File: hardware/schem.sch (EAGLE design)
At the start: 19 parts, among them IC1 7805L, IC2 L298, U2 TINY85-20-DIP

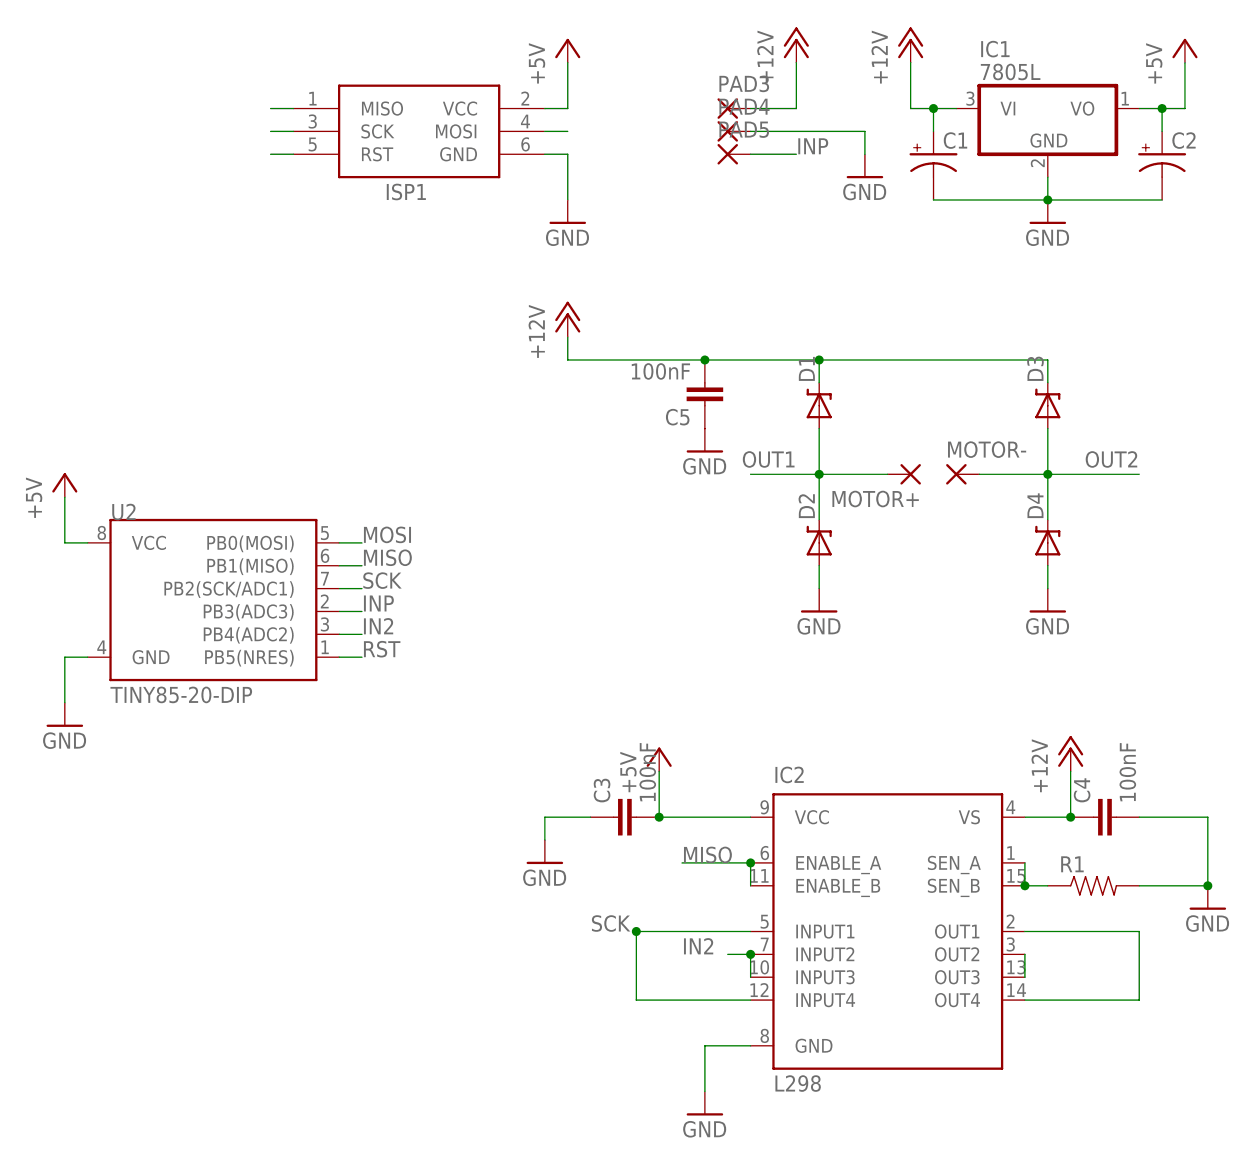
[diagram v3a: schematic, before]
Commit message: Routed board
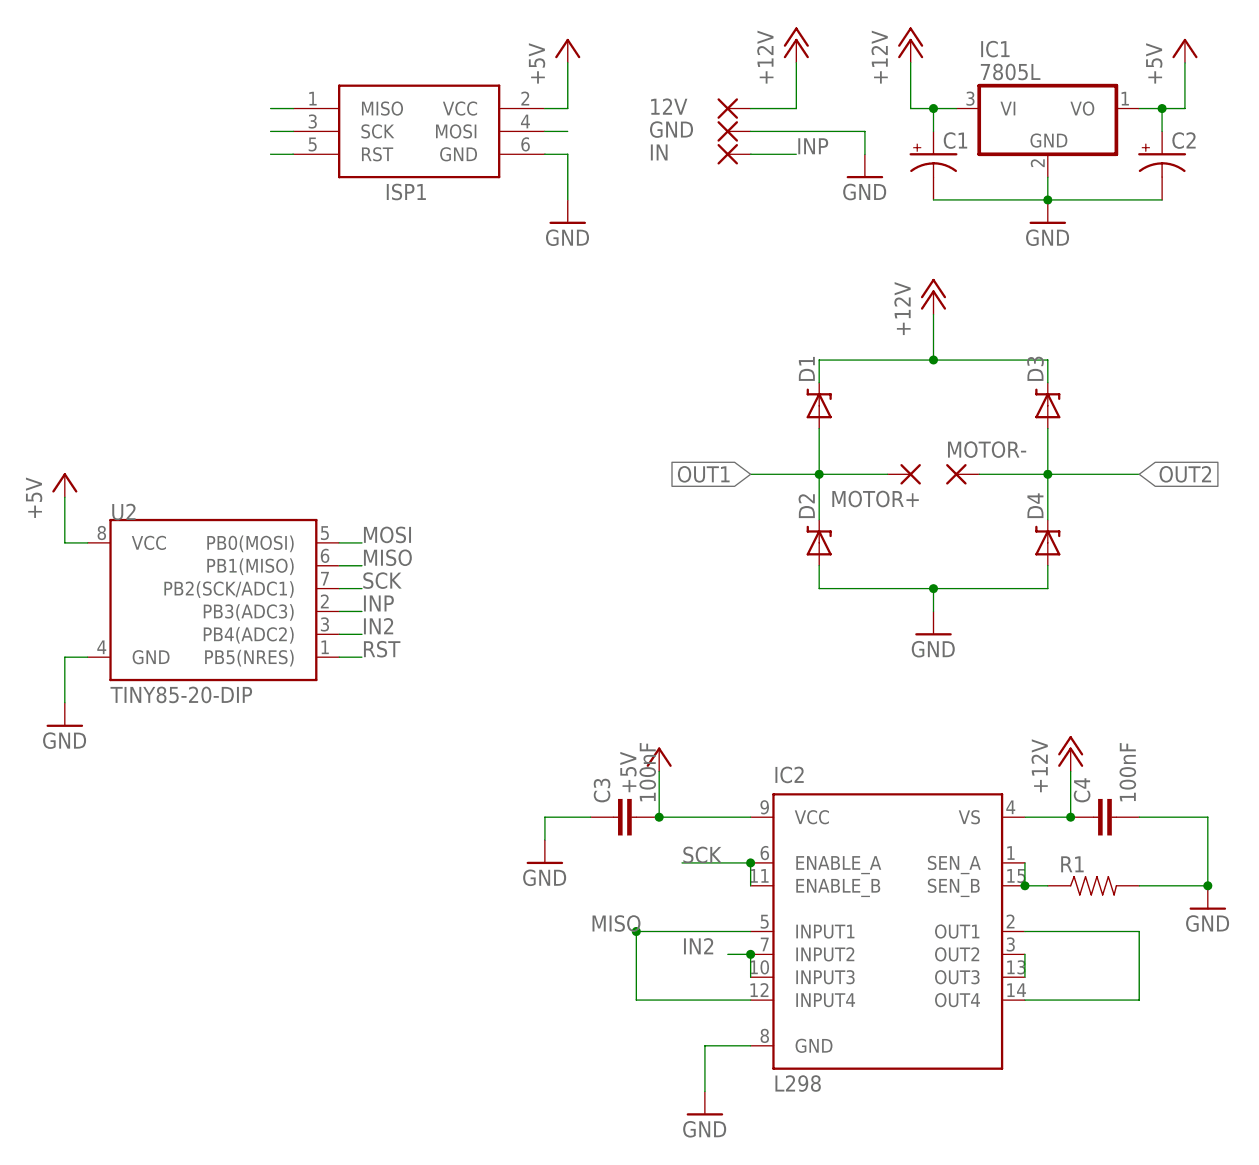
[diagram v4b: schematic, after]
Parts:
- removed C5: 100nF, SparkFun-Capacitors:CAPPTH2
- renumbered PAD3 to 12V, PAD4 to GND, PAD5 to IN
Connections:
- net +12V: no longer C5.2
- net GND: no longer C5.1
- net MISO: now also IC2.INPUT1, IC2.INPUT4; no longer IC2.ENABLE_A, IC2.ENABLE_B
- net SCK: now also IC2.ENABLE_A, IC2.ENABLE_B; no longer IC2.INPUT1, IC2.INPUT4
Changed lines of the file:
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@@
 <part name="MOTOR+" library="wirepad" deviceset="3,81/1,4" device=""/>
 <part name="MOTOR-" library="wirepad" deviceset="3,81/1,4" device=""/>
-<part name="PAD3" library="wirepad" deviceset="3,81/1,4" device=""/>
-<part name="PAD4" library="wirepad" deviceset="3,81/1,4" device=""/>
-<part name="PAD5" library="wirepad" deviceset="1,6/0,9" device=""/>
+<part name="12V" library="wirepad" deviceset="3,81/1,4" device=""/>
+<part name="GND" library="wirepad" deviceset="3,81/1,4" device=""/>
+<part name="IN" library="wirepad" deviceset="1,6/0,9" device=""/>
 <part name="C1" library="adafruit" deviceset="CPOL-US" device="E2.5-6"/>
 <part name="C2" library="adafruit" deviceset="CPOL-US" device="E2.5-6"/>
@@
 <part name="D3" library="SparkFun-DiscreteSemi" deviceset="DIODE-ZENER" device="PTH"/>
 <part name="D4" library="SparkFun-DiscreteSemi" deviceset="DIODE-ZENER" device="PTH"/>
+<part name="P+8" library="supply1" deviceset="+12V" device=""/>
 <part name="GND8" library="supply1" deviceset="GND" device=""/>
-<part name="GND9" library="supply1" deviceset="GND" device=""/>
-<part name="C5" library="SparkFun-Capacitors" deviceset="CAP" device="PTH2" value="100nF"/>
-<part name="GND10" library="supply1" deviceset="GND" device=""/>
-<part name="P+8" library="supply1" deviceset="+12V" device=""/>
 </parts>
 <sheets>
@@
 <instance part="MOTOR+" gate="1" x="149.86" y="58.42" rot="R180"/>
 <instance part="MOTOR-" gate="1" x="154.94" y="58.42"/>
-<instance part="PAD3" gate="1" x="129.54" y="99.06"/>
-<instance part="PAD4" gate="1" x="129.54" y="96.52"/>
-<instance part="PAD5" gate="1" x="129.54" y="93.98"/>
+<instance part="12V" gate="1" x="129.54" y="99.06" smashed="yes">
+<attribute name="NAME" x="120.777" y="98.3742" size="1.778" layer="95"/>
+<attribute name="VALUE" x="128.397" y="95.758" size="1.778" layer="96"/>
+</instance>
+<instance part="GND" gate="1" x="129.54" y="96.52" smashed="yes">
+<attribute name="NAME" x="120.777" y="95.8342" size="1.778" layer="95"/>
+<attribute name="VALUE" x="128.397" y="93.218" size="1.778" layer="96"/>
+</instance>
+<instance part="IN" gate="1" x="129.54" y="93.98" smashed="yes">
+<attribute name="NAME" x="120.777" y="93.2942" size="1.778" layer="95"/>
+<attribute name="VALUE" x="128.397" y="90.678" size="1.778" layer="96"/>
+</instance>
 <instance part="C1" gate="G$1" x="152.4" y="93.98"/>
 <instance part="C2" gate="G$1" x="177.8" y="93.98"/>
@@
 <attribute name="NAME" x="164.6174" y="53.34" size="1.778" layer="95" rot="R90"/>
 </instance>
-<instance part="GND8" gate="1" x="139.7" y="43.18"/>
-<instance part="GND9" gate="1" x="165.1" y="43.18"/>
-<instance part="C5" gate="G$1" x="127" y="68.58" rot="R180"/>
-<instance part="GND10" gate="1" x="127" y="60.96"/>
-<instance part="P+8" gate="1" x="111.76" y="76.2"/>
+<instance part="P+8" gate="1" x="152.4" y="78.74"/>
+<instance part="GND8" gate="1" x="152.4" y="40.64"/>
 </instances>
 <busses>
@@
 <wire x1="137.16" y1="104.14" x2="137.16" y2="99.06" width="0.1524" layer="91"/>
 <wire x1="137.16" y1="99.06" x2="132.08" y2="99.06" width="0.1524" layer="91"/>
-<pinref part="PAD3" gate="1" pin="P"/>
+<pinref part="12V" gate="1" pin="P"/>
 </segment>
 <segment>
@@
 <pinref part="D3" gate="G$1" pin="C"/>
 <wire x1="165.1" y1="68.58" x2="165.1" y2="71.12" width="0.1524" layer="91"/>
-<wire x1="165.1" y1="71.12" x2="139.7" y2="71.12" width="0.1524" layer="91"/>
-<wire x1="127" y1="71.12" x2="139.7" y2="71.12" width="0.1524" layer="91"/>
+<wire x1="165.1" y1="71.12" x2="152.4" y2="71.12" width="0.1524" layer="91"/>
+<wire x1="152.4" y1="71.12" x2="152.4" y2="76.2" width="0.1524" layer="91"/>
+<pinref part="P+8" gate="1" pin="+12V"/>
 <pinref part="D1" gate="G$1" pin="C"/>
 <wire x1="139.7" y1="68.58" x2="139.7" y2="71.12" width="0.1524" layer="91"/>
-<junction x="139.7" y="71.12"/>
-<pinref part="C5" gate="G$1" pin="2"/>
-<wire x1="127" y1="71.12" x2="111.76" y2="71.12" width="0.1524" layer="91"/>
-<junction x="127" y="71.12"/>
-<wire x1="111.76" y1="71.12" x2="111.76" y2="73.66" width="0.1524" layer="91"/>
-<pinref part="P+8" gate="1" pin="+12V"/>
+<wire x1="152.4" y1="71.12" x2="139.7" y2="71.12" width="0.1524" layer="91"/>
+<junction x="152.4" y="71.12"/>
 </segment>
 </net>
@@
 <pinref part="GND1" gate="1" pin="GND"/>
 <wire x1="144.78" y1="96.52" x2="144.78" y2="93.98" width="0.1524" layer="91"/>
-<pinref part="PAD4" gate="1" pin="P"/>
+<pinref part="GND" gate="1" pin="P"/>
 </segment>
 <segment>
@@
 </segment>
 <segment>
+<pinref part="D4" gate="G$1" pin="A"/>
+<wire x1="165.1" y1="48.26" x2="165.1" y2="45.72" width="0.1524" layer="91"/>
 <pinref part="D2" gate="G$1" pin="A"/>
 <wire x1="139.7" y1="48.26" x2="139.7" y2="45.72" width="0.1524" layer="91"/>
+<wire x1="165.1" y1="45.72" x2="152.4" y2="45.72" width="0.1524" layer="91"/>
 <pinref part="GND8" gate="1" pin="GND"/>
-</segment>
-<segment>
-<pinref part="D4" gate="G$1" pin="A"/>
-<wire x1="165.1" y1="48.26" x2="165.1" y2="45.72" width="0.1524" layer="91"/>
-<pinref part="GND9" gate="1" pin="GND"/>
-</segment>
-<segment>
-<pinref part="C5" gate="G$1" pin="1"/>
-<pinref part="GND10" gate="1" pin="GND"/>
+<wire x1="152.4" y1="45.72" x2="139.7" y2="45.72" width="0.1524" layer="91"/>
+<wire x1="152.4" y1="45.72" x2="152.4" y2="43.18" width="0.1524" layer="91"/>
+<junction x="152.4" y="45.72"/>
 </segment>
 </net>
@@
 <wire x1="132.08" y1="93.98" x2="137.16" y2="93.98" width="0.1524" layer="91"/>
 <label x="137.16" y="93.98" size="1.778" layer="95"/>
-<pinref part="PAD5" gate="1" pin="P"/>
+<pinref part="IN" gate="1" pin="P"/>
 </segment>
 </net>
@@
 <pinref part="ISP1" gate="G$1" pin="MISO"/>
 <wire x1="78.74" y1="99.06" x2="81.28" y2="99.06" width="0.1524" layer="91"/>
-</segment>
-<segment>
-<pinref part="IC2" gate="L298" pin="ENABLE_A"/>
-<pinref part="IC2" gate="L298" pin="ENABLE_B"/>
-<wire x1="132.08" y1="15.24" x2="132.08" y2="12.7" width="0.1524" layer="91"/>
-<wire x1="132.08" y1="15.24" x2="124.46" y2="15.24" width="0.1524" layer="91"/>
-<junction x="132.08" y="15.24"/>
-<label x="124.46" y="15.24" size="1.778" layer="95"/>
-</segment>
-</net>
-<net name="RST" class="0">
-<segment>
-<pinref part="U2" gate="G$1" pin="PB5(NRES)"/>
-<wire x1="86.36" y1="38.1" x2="88.9" y2="38.1" width="0.1524" layer="91"/>
-<label x="88.9" y="38.1" size="1.778" layer="95"/>
-</segment>
-<segment>
-<pinref part="ISP1" gate="G$1" pin="RST"/>
-<wire x1="81.28" y1="93.98" x2="78.74" y2="93.98" width="0.1524" layer="91"/>
-</segment>
-</net>
-<net name="SCK" class="0">
-<segment>
-<pinref part="ISP1" gate="G$1" pin="SCK"/>
-<wire x1="81.28" y1="96.52" x2="78.74" y2="96.52" width="0.1524" layer="91"/>
-</segment>
-<segment>
-<pinref part="U2" gate="G$1" pin="PB2(SCK/ADC1)"/>
-<wire x1="86.36" y1="45.72" x2="88.9" y2="45.72" width="0.1524" layer="91"/>
-<label x="88.9" y="45.72" size="1.778" layer="95"/>
 </segment>
 <segment>
@@
 <junction x="119.38" y="7.62"/>
 <label x="114.3" y="7.62" size="1.778" layer="95"/>
+</segment>
+</net>
+<net name="RST" class="0">
+<segment>
+<pinref part="U2" gate="G$1" pin="PB5(NRES)"/>
+<wire x1="86.36" y1="38.1" x2="88.9" y2="38.1" width="0.1524" layer="91"/>
+<label x="88.9" y="38.1" size="1.778" layer="95"/>
+</segment>
+<segment>
+<pinref part="ISP1" gate="G$1" pin="RST"/>
+<wire x1="81.28" y1="93.98" x2="78.74" y2="93.98" width="0.1524" layer="91"/>
+</segment>
+</net>
+<net name="SCK" class="0">
+<segment>
+<pinref part="ISP1" gate="G$1" pin="SCK"/>
+<wire x1="81.28" y1="96.52" x2="78.74" y2="96.52" width="0.1524" layer="91"/>
+</segment>
+<segment>
+<pinref part="U2" gate="G$1" pin="PB2(SCK/ADC1)"/>
+<wire x1="86.36" y1="45.72" x2="88.9" y2="45.72" width="0.1524" layer="91"/>
+<label x="88.9" y="45.72" size="1.778" layer="95"/>
+</segment>
+<segment>
+<pinref part="IC2" gate="L298" pin="ENABLE_A"/>
+<pinref part="IC2" gate="L298" pin="ENABLE_B"/>
+<wire x1="132.08" y1="15.24" x2="132.08" y2="12.7" width="0.1524" layer="91"/>
+<wire x1="132.08" y1="15.24" x2="124.46" y2="15.24" width="0.1524" layer="91"/>
+<junction x="132.08" y="15.24"/>
+<label x="124.46" y="15.24" size="1.778" layer="95"/>
 </segment>
 </net>
@@
 <pinref part="D4" gate="G$1" pin="C"/>
 <wire x1="165.1" y1="58.42" x2="165.1" y2="53.34" width="0.1524" layer="91"/>
-<label x="175.26" y="60.96" size="1.778" layer="95" rot="R180"/>
+<label x="175.26" y="58.42" size="1.778" layer="95" xref="yes"/>
 </segment>
 </net>
@@
 <pinref part="D1" gate="G$1" pin="A"/>
 <wire x1="139.7" y1="58.42" x2="139.7" y2="63.5" width="0.1524" layer="91"/>
-<label x="137.16" y="60.96" size="1.778" layer="95" rot="R180"/>
-</segment>
-</net>
+<label x="132.08" y="58.42" size="1.778" layer="95" rot="R180" xref="yes"/>
+</segment>
+</net>

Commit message: Updated silk screen and moved components on board
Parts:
- renumbered ISP1 to PRG
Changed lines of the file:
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@@
 <parts>
 <part name="IC1" library="linear" deviceset="78*" device="L" technology="05"/>
-<part name="ISP1" library="adafruit" deviceset="AVRISP" device="-6"/>
+<part name="PRG" library="adafruit" deviceset="AVRISP" device="-6"/>
 <part name="P+1" library="supply1" deviceset="+12V" device=""/>
 <part name="GND1" library="supply1" deviceset="GND" device=""/>
@@
 <instances>
 <instance part="IC1" gate="A1" x="165.1" y="99.06"/>
-<instance part="ISP1" gate="G$1" x="93.98" y="96.52"/>
+<instance part="PRG" gate="G$1" x="93.98" y="96.52"/>
 <instance part="P+1" gate="1" x="137.16" y="106.68"/>
 <instance part="GND1" gate="1" x="144.78" y="91.44"/>
@@
 </segment>
 <segment>
-<pinref part="ISP1" gate="G$1" pin="GND"/>
+<pinref part="PRG" gate="G$1" pin="GND"/>
 <wire x1="109.22" y1="93.98" x2="111.76" y2="93.98" width="0.1524" layer="91"/>
 <wire x1="111.76" y1="93.98" x2="111.76" y2="88.9" width="0.1524" layer="91"/>
@@
 </segment>
 <segment>
-<pinref part="ISP1" gate="G$1" pin="VCC"/>
+<pinref part="PRG" gate="G$1" pin="VCC"/>
 <wire x1="109.22" y1="99.06" x2="111.76" y2="99.06" width="0.1524" layer="91"/>
 <wire x1="111.76" y1="99.06" x2="111.76" y2="104.14" width="0.1524" layer="91"/>
@@
 <net name="MOSI" class="0">
 <segment>
-<pinref part="ISP1" gate="G$1" pin="MOSI"/>
+<pinref part="PRG" gate="G$1" pin="MOSI"/>
 <wire x1="109.22" y1="96.52" x2="111.76" y2="96.52" width="0.1524" layer="91"/>
 </segment>
@@
 </segment>
 <segment>
-<pinref part="ISP1" gate="G$1" pin="MISO"/>
+<pinref part="PRG" gate="G$1" pin="MISO"/>
 <wire x1="78.74" y1="99.06" x2="81.28" y2="99.06" width="0.1524" layer="91"/>
 </segment>
@@
 </segment>
 <segment>
-<pinref part="ISP1" gate="G$1" pin="RST"/>
+<pinref part="PRG" gate="G$1" pin="RST"/>
 <wire x1="81.28" y1="93.98" x2="78.74" y2="93.98" width="0.1524" layer="91"/>
 </segment>
@@
 <net name="SCK" class="0">
 <segment>
-<pinref part="ISP1" gate="G$1" pin="SCK"/>
+<pinref part="PRG" gate="G$1" pin="SCK"/>
 <wire x1="81.28" y1="96.52" x2="78.74" y2="96.52" width="0.1524" layer="91"/>
 </segment>

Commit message: Cleaned up board and moved around components
Made space to give H Bridge room to breath

Imporved Silk Screen
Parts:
- renumbered D1 to DIODE1, D2 to DIODE2, D3 to DIODE3, D4 to DIODE4
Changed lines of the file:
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@@
 <part name="GND7" library="supply1" deviceset="GND" device=""/>
 <part name="R1" library="SparkFun-Passives" deviceset="RESISTOR" device="PTH-1/4W"/>
-<part name="D1" library="SparkFun-DiscreteSemi" deviceset="DIODE-ZENER" device="PTH"/>
-<part name="D2" library="SparkFun-DiscreteSemi" deviceset="DIODE-ZENER" device="PTH"/>
-<part name="D3" library="SparkFun-DiscreteSemi" deviceset="DIODE-ZENER" device="PTH"/>
-<part name="D4" library="SparkFun-DiscreteSemi" deviceset="DIODE-ZENER" device="PTH"/>
+<part name="DIODE1" library="SparkFun-DiscreteSemi" deviceset="DIODE-ZENER" device="PTH"/>
+<part name="DIODE2" library="SparkFun-DiscreteSemi" deviceset="DIODE-ZENER" device="PTH"/>
+<part name="DIODE3" library="SparkFun-DiscreteSemi" deviceset="DIODE-ZENER" device="PTH"/>
+<part name="DIODE4" library="SparkFun-DiscreteSemi" deviceset="DIODE-ZENER" device="PTH"/>
 <part name="P+8" library="supply1" deviceset="+12V" device=""/>
 <part name="GND8" library="supply1" deviceset="GND" device=""/>
@@
 <instance part="GND7" gate="1" x="127" y="-12.7"/>
 <instance part="R1" gate="G$1" x="170.18" y="12.7"/>
-<instance part="D1" gate="G$1" x="139.7" y="66.04" smashed="yes" rot="R90">
+<instance part="DIODE1" gate="G$1" x="139.7" y="66.04" smashed="yes" rot="R90">
 <attribute name="NAME" x="139.2174" y="68.58" size="1.778" layer="95" rot="R90"/>
 </instance>
-<instance part="D2" gate="G$1" x="139.7" y="50.8" smashed="yes" rot="R90">
+<instance part="DIODE2" gate="G$1" x="139.7" y="50.8" smashed="yes" rot="R90">
 <attribute name="NAME" x="139.2174" y="53.34" size="1.778" layer="95" rot="R90"/>
 </instance>
-<instance part="D3" gate="G$1" x="165.1" y="66.04" smashed="yes" rot="R90">
+<instance part="DIODE3" gate="G$1" x="165.1" y="66.04" smashed="yes" rot="R90">
 <attribute name="NAME" x="164.6174" y="68.58" size="1.778" layer="95" rot="R90"/>
 </instance>
-<instance part="D4" gate="G$1" x="165.1" y="50.8" smashed="yes" rot="R90">
+<instance part="DIODE4" gate="G$1" x="165.1" y="50.8" smashed="yes" rot="R90">
 <attribute name="NAME" x="164.6174" y="53.34" size="1.778" layer="95" rot="R90"/>
 </instance>
@@
 </segment>
 <segment>
-<pinref part="D3" gate="G$1" pin="C"/>
+<pinref part="DIODE3" gate="G$1" pin="C"/>
 <wire x1="165.1" y1="68.58" x2="165.1" y2="71.12" width="0.1524" layer="91"/>
 <wire x1="165.1" y1="71.12" x2="152.4" y2="71.12" width="0.1524" layer="91"/>
 <wire x1="152.4" y1="71.12" x2="152.4" y2="76.2" width="0.1524" layer="91"/>
 <pinref part="P+8" gate="1" pin="+12V"/>
-<pinref part="D1" gate="G$1" pin="C"/>
+<pinref part="DIODE1" gate="G$1" pin="C"/>
 <wire x1="139.7" y1="68.58" x2="139.7" y2="71.12" width="0.1524" layer="91"/>
 <wire x1="152.4" y1="71.12" x2="139.7" y2="71.12" width="0.1524" layer="91"/>
@@
 </segment>
 <segment>
-<pinref part="D4" gate="G$1" pin="A"/>
+<pinref part="DIODE4" gate="G$1" pin="A"/>
 <wire x1="165.1" y1="48.26" x2="165.1" y2="45.72" width="0.1524" layer="91"/>
-<pinref part="D2" gate="G$1" pin="A"/>
+<pinref part="DIODE2" gate="G$1" pin="A"/>
 <wire x1="139.7" y1="48.26" x2="139.7" y2="45.72" width="0.1524" layer="91"/>
 <wire x1="165.1" y1="45.72" x2="152.4" y2="45.72" width="0.1524" layer="91"/>
@@
 <pinref part="MOTOR-" gate="1" pin="P"/>
 <wire x1="157.48" y1="58.42" x2="165.1" y2="58.42" width="0.1524" layer="91"/>
-<pinref part="D3" gate="G$1" pin="A"/>
+<pinref part="DIODE3" gate="G$1" pin="A"/>
 <wire x1="165.1" y1="58.42" x2="175.26" y2="58.42" width="0.1524" layer="91"/>
 <wire x1="165.1" y1="63.5" x2="165.1" y2="58.42" width="0.1524" layer="91"/>
 <junction x="165.1" y="58.42"/>
-<pinref part="D4" gate="G$1" pin="C"/>
+<pinref part="DIODE4" gate="G$1" pin="C"/>
 <wire x1="165.1" y1="58.42" x2="165.1" y2="53.34" width="0.1524" layer="91"/>
 <label x="175.26" y="58.42" size="1.778" layer="95" xref="yes"/>
@@
 <pinref part="MOTOR+" gate="1" pin="P"/>
 <wire x1="147.32" y1="58.42" x2="139.7" y2="58.42" width="0.1524" layer="91"/>
-<pinref part="D2" gate="G$1" pin="C"/>
+<pinref part="DIODE2" gate="G$1" pin="C"/>
 <wire x1="139.7" y1="58.42" x2="132.08" y2="58.42" width="0.1524" layer="91"/>
 <wire x1="139.7" y1="53.34" x2="139.7" y2="58.42" width="0.1524" layer="91"/>
 <junction x="139.7" y="58.42"/>
-<pinref part="D1" gate="G$1" pin="A"/>
+<pinref part="DIODE1" gate="G$1" pin="A"/>
 <wire x1="139.7" y1="58.42" x2="139.7" y2="63.5" width="0.1524" layer="91"/>
 <label x="132.08" y="58.42" size="1.778" layer="95" rot="R180" xref="yes"/>
